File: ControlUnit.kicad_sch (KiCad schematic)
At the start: 20 parts, among them M1 Motor_DC_ALT, Q1 IRLZ44N, SW2 SW_DPST_x2, U3 PIC24HJ128GP502, U5 DRV8871DDA, U6 INA180A1, U7 VL53L0CXV0DH1

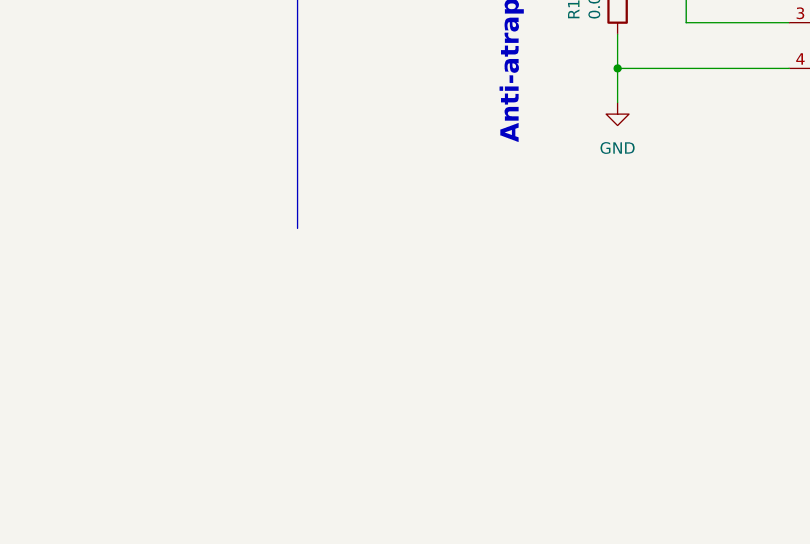
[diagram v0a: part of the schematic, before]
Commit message: Actualització projecte KiCad
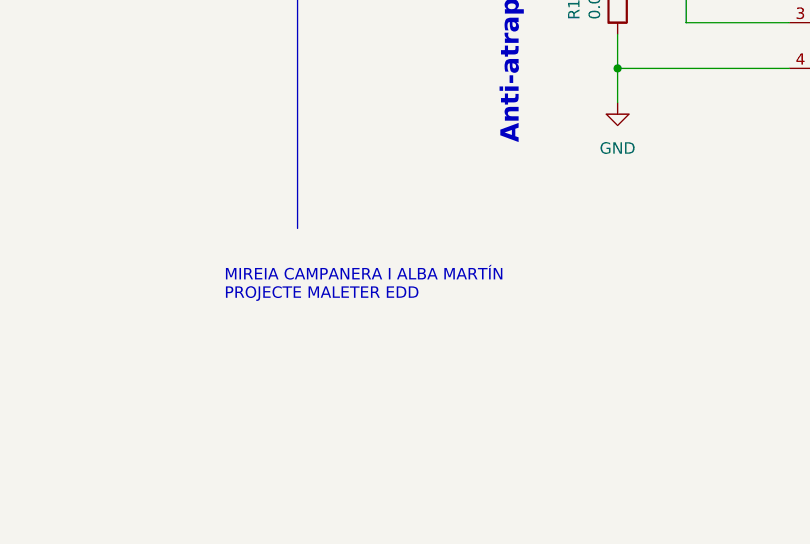
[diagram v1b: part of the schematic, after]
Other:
- note added: "MIREIA CAMPANERA I ALBA MARTÍN PROJECTE MALETER EDD"

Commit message: Neteja carpeta
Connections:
- net 3.3V: now also C6.1, U3.13 (VDD)
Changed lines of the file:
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@@
 	(global_label "3.3V"
 		(shape input)
-		(at 86.36 125.73 270)
+		(at 85.09 125.73 270)
 		(fields_autoplaced yes)
 		(effects
@@
 		)
 		(property "Intersheetrefs" "${INTERSHEET_REFS}"
-			(at 86.36 133.3036 90)
+			(at 85.09 133.3036 90)
 			(effects
 				(font

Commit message: Definició parcial huellas
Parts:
- C5, C6, C7, C8: footprint (none) -> Capacitor_SMD:C_0201_0603Metric
- R1, R10, R11, R2, R3, R4, R5, R6: footprint (none) -> Resistor_SMD:R_0201_0603Metric
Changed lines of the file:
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@@
 			)
 		)
-		(property "Footprint" ""
+		(property "Footprint" "Resistor_SMD:R_0201_0603Metric"
 			(at 224.028 139.7 90)
 			(effects
@@
 			)
 		)
-		(property "Footprint" ""
+		(property "Footprint" "Resistor_SMD:R_0201_0603Metric"
 			(at 32.512 31.75 90)
 			(effects
@@
 			)
 		)
-		(property "Footprint" ""
+		(property "Footprint" "Capacitor_SMD:C_0201_0603Metric"
 			(at 92.71 114.6048 0)
 			(effects
@@
 			)
 		)
-		(property "Footprint" ""
+		(property "Footprint" "Resistor_SMD:R_0201_0603Metric"
 			(at 124.46 161.798 90)
 			(effects
@@
 			)
 		)
-		(property "Footprint" ""
+		(property "Footprint" "Resistor_SMD:R_0201_0603Metric"
 			(at 217.932 71.12 90)
 			(effects
@@
 			)
 		)
-		(property "Footprint" ""
+		(property "Footprint" "Capacitor_SMD:C_0201_0603Metric"
 			(at 101.6 34.5948 0)
 			(effects
@@
 			)
 		)
-		(property "Footprint" ""
+		(property "Footprint" "Capacitor_SMD:C_0201_0603Metric"
 			(at 82.2452 43.18 0)
 			(effects
@@
 			)
 		)
-		(property "Footprint" ""
+		(property "Footprint" "Resistor_SMD:R_0201_0603Metric"
 			(at 153.162 92.71 90)
 			(effects
@@
 			)
 		)
-		(property "Footprint" ""
+		(property "Footprint" "Resistor_SMD:R_0201_0603Metric"
 			(at 168.402 95.25 90)
 			(effects
@@
 			)
 		)
-		(property "Footprint" ""
+		(property "Footprint" "Capacitor_SMD:C_0201_0603Metric"
 			(at 35.2552 50.8 0)
 			(effects
@@
 			)
 		)
-		(property "Footprint" ""
+		(property "Footprint" "Resistor_SMD:R_0201_0603Metric"
 			(at 43.18 42.418 90)
 			(effects
@@
 			)
 		)
-		(property "Footprint" ""
+		(property "Footprint" "Resistor_SMD:R_0201_0603Metric"
 			(at 39.37 165.608 90)
 			(effects

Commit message: Botonera
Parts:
- added R12, R13: 10kΩ, Resistor_SMD:R_0201_0603Metric, symbol Device:R
- added SW1, SW3: SW_DPST_x2, Button_Switch_SMD:SW_DIP_SPSTx02_Slide_6.7x6.64mm_W6.73mm_P2.54mm_LowProfile_JPin, symbol Switch:SW_DPST_x2
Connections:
- net 3.3V: now also R12.1, R13.1
- net FinalCarrera: now also SW2.1 (A); no longer SW2.2 (B)
- net GND: now also SW2.2 (B), SW1.2 (B), SW3.2 (B); no longer SW2.1 (A)
- net Calefactor: now reaches U3.6 (AN4/C1IN-/RP2/CN6/RB2)
- net Calefactor: now also R13.2, SW3.1 (A)
- net ON/OFF: now reaches U3.7 (AN5/C1IN+/RP3/CN7/RB3)
- net ON/OFF: now also R12.2, SW1.1 (A)
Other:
- note added: "Botonera"
- moved on the sheet: Q1, R3, R6, R9, SW2A

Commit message: coses que falten
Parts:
- removed SW2: SW_DPST_x2, symbol Switch:SW_DPST_x2
- added C14, C15: 22pF, Capacitor_SMD:C_0201_0603Metric, symbol Device:C
- added J4: Conn_01x05_Pin, Connector_PinSocket_1.27mm:PinSocket_1x05_P1.27mm_Vertical, symbol Connector:Conn_01x05_Pin
- added SW4: SW_SPDT, Button_Switch_THT:SW_XKB_DM1-16UP-1, symbol Switch:SW_SPDT
- added Y1: 8MHz, Crystal:Crystal_HC49-4H_Vertical, symbol Device:Crystal
- M1: footprint (none) -> TerminalBlock_CUI:TerminalBlock_CUI_TB007-508-02_1x02_P5.08mm_Horizontal
- R9: footprint (none) -> Resistor_SMD:R_0201_0603Metric
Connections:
- net 3.3V: now also J4.3 (Pin_3)
- net FinalCarrera: now also SW4.2 (B)
- net GND: now also C14.2, C15.2, J4.4 (Pin_4), SW4.1 (A)
- net MCLR: now reaches R5.2, U3.1 (~{MCLR})
- net MCLR: now also J4.5 (Pin_5)
- net at U3.10 (OSC2/CLKO/CN29/PMA0/RA3): now also C15.1, Y1.1
- net PGD: now reaches U3.21 (PGED2/TDI/RP10/CN16/PMD2/RB10)
- net PGD: now also J4.2 (Pin_2)
- net PGC: now reaches U3.22 (PGEC2/TMS/RP11/CN15/PMD1/RB11)
- net PGC: now also J4.1 (Pin_1)
- net at U3.9 (OSC1/CLKI/CN30/RA2): now also C14.1, Y1.2
- no-connect marks 0 -> 1

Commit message: Correccions professor
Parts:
- added C16: 0.1uF, Capacitor_SMD:C_0201_0603Metric, symbol Device:C
- added R14: 15k, Resistor_SMD:R_0201_0603Metric, symbol Device:R
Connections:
- net +12V: now also C16.2
- net 3.3V: now also R1.1, R2.1
- net GND: now also C16.1, R14.2
- net SCL: now also R1.2, U3.17 (RB8); no longer R1.1
- net SDA: now also R2.2, U3.18 (RB9); no longer R2.1
- net at U5.4 (ILIM): now also R14.1
- no-connect marks 1 -> 12
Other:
- note added: "MIREIA CAMPANERA I ALBA MARTÍN PROJECTE MALETER EDD Microcontrolador, sensor final de carrera, sensor de peu, motor del maleter i botonera"
- note removed: "MIREIA CAMPANERA I ALBA MARTÍN PROJECTE MALETER EDD"
- moved on the sheet: C14, C15, C5, C6, C7, C8, J4, M1, Q1, R1, R10, R11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

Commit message: Ultima versio projecte
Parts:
- removed C16: 0.1uF, Capacitor_SMD:C_0201_0603Metric, symbol Device:C
- removed M1: Motor_DC_ALT, TerminalBlock_CUI:TerminalBlock_CUI_TB007-508-02_1x02_P5.08mm_Horizontal, symbol Motor:Motor_DC_ALT
- removed R10: 0.05, Resistor_SMD:R_0201_0603Metric, symbol Device:R
- removed R14: 15k, Resistor_SMD:R_0201_0603Metric, symbol Device:R
- removed SW4: SW_SPDT, Button_Switch_THT:SW_XKB_DM1-16UP-1, symbol Switch:SW_SPDT
- removed U5: DRV8871DDA, Package_SO:Texas_HTSOP-8-1EP_3.9x4.9mm_P1.27mm_EP2.95x4.9mm_Mask2.4x3.1mm_ThermalVias, symbol Driver_Motor:DRV8871DDA
- removed U6: INA180A1, Package_TO_SOT_SMD:SOT-23-5, symbol Amplifier_Current:INA180A1
- added C10, C11, C12, C13, C9: 100nF, Capacitor_SMD:C_0201_0603Metric, symbol Device:C
- added C17: 0.1uF, Capacitor_SMD:C_0201_0603Metric, symbol Device:C
- added D3: LED, LED_SMD:LED_0201_0603Metric, symbol Device:LED
- added FB1: FerriteBead, symbol Device:FerriteBead
- added J2, J3: DE9_Pins, Connector_Dsub:DSUB-9_Pins_Horizontal_P2.77x2.84mm_EdgePinOffset9.40mm, symbol Connector:DE9_Pins
- added R16: 150, Resistor_SMD:R_0201_0603Metric, symbol Device:R
- added R7: 120Ω, Resistor_SMD:R_0201_0603Metric, symbol Device:R
- added R8: 10k, Resistor_SMD:R_0201_0603Metric, symbol Device:R
- added SW2: SW_DPST_x2, Button_Switch_SMD:SW_DIP_SPSTx02_Slide_6.7x6.64mm_W6.73mm_P2.54mm_LowProfile_JPin, symbol Switch:SW_DPST_x2
- added SW5: SW_Push, symbol Switch:SW_Push
- added U4: MCP2551-I-SN, Package_SO:SOIC-8_3.9x4.9mm_P1.27mm, symbol Interface_CAN_LIN:MCP2551-I-SN
- added U8: MAX3232, Package_SO:SOIC-16W_5.3x10.2mm_P1.27mm, symbol Interface_UART:MAX3232
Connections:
- net 3.3V: now also C13.1, C17.1, FB1.1, U8.16 (VCC); no longer C7.1, U3.28 (RB7/PGD)
- net FinalCarrera: now also SW2.1 (A)
- net GND: now also C13.2, C17.2, C9.2, J2.3, J3.5, R16.2, R8.2, SW2.2 (B), SW5.1, U4.2 (VSS), U8.15 (GND); no longer U3.19 (VSS)
- net at C5.1, R4.2, R5.1: now also SW5.2
- net at U3.24 (RB13): now also D3.2 (A)
- new net: C11.1, U8.4 (C2+)
- new net: C11.2, U8.5 (C2-)
- new net: C12.1, U8.1 (C1+)
- new net: C10.1, U8.2 (VS+)
- new net: C12.2, U8.3 (C1-)
- new net: C10.2, U8.6 (VS-)
- new net: C7.1, FB1.2, U3.28 (RB7/PGD)
- new net: R8.1, U4.8 (Rs)
- new net: D3.1 (K), R16.1
- new net +5V: C9.1, U4.3 (VDD)
- new net CANH: J2.7, R7.1, U4.7 (CANH)
- new net CANL: J2.2, R7.2, U4.6 (CANL)
- new net RX: J3.3, U8.12 (R1OUT)
- new net RX_CAN: U4.4 (RXD)
- new net RX_USART: U8.13 (R1IN)
- new net TX: J3.2, U8.14 (T1OUT)
- new net TX_CAN: U4.1 (TXD)
- new net TX_USART: U8.11 (T1IN)
- no-connect marks 12 -> 27
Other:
- note added: "BUS CAN"
- note added: "LED"
- note added: "MIREIA CAMPANERA I ALBA MARTÍN PROJECTE MALETER EDD Microcontrolador, sensor final de carrera, sensor de peu, comunicacions i botonera"
- note added: "USART"
- note added: "vermell"
- note removed: "Anti-atrapament"
- note removed: "MIREIA CAMPANERA I ALBA MARTÍN PROJECTE MALETER EDD Microcontrolador, sensor final de carrera, sensor de peu, motor del maleter i botonera"
- note removed: "Motor del maleter"
- moved on the sheet: C15, J4, Q1, R1, R2, R3, R6, R9

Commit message: abc
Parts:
- FB1: footprint (none) -> Inductor_SMD:L_0201_0603Metric
- SW5: footprint (none) -> Button_Switch_THT:SW_PUSH_6mm
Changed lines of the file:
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@@
 			)
 		)
-		(property "Footprint" ""
+		(property "Footprint" "Button_Switch_THT:SW_PUSH_6mm"
 			(at 73.66 74.93 0)
 			(effects
@@
 			)
 		)
-		(property "Footprint" ""
+		(property "Footprint" "Inductor_SMD:L_0201_0603Metric"
 			(at 142.748 58.42 90)
 			(effects
